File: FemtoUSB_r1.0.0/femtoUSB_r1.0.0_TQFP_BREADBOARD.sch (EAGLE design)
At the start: 26 parts, among them IC1 ATSAMD21E18A-AU

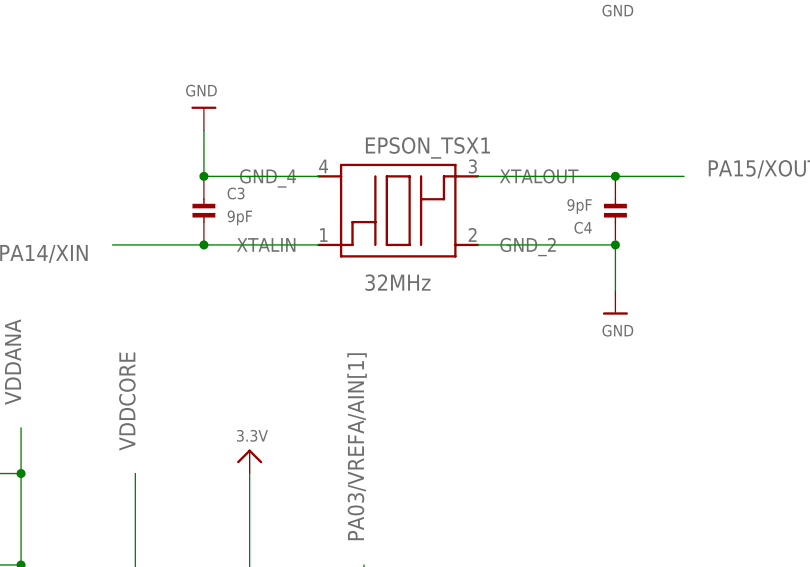
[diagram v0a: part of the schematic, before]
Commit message: Updating gerbers and BoM/Partslist of QFN version
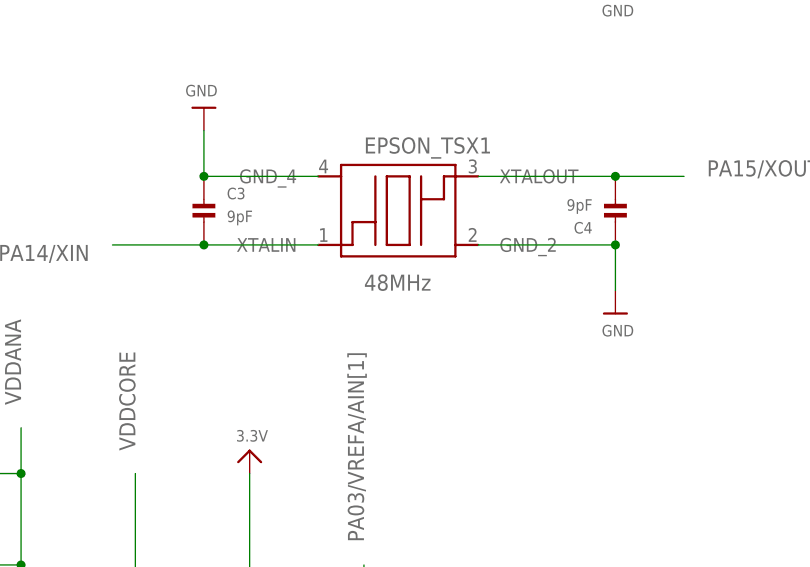
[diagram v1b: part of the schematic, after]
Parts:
- EPSON_TSX1: value 32MHz -> 48MHz
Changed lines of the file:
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@@
 <part name="U$24" library="microbuilder" deviceset="GND" device=""/>
 <part name="U$25" library="microbuilder" deviceset="GND" device=""/>
-<part name="EPSON_TSX1" library="crystals" deviceset="TSX-3225" device="" value="32MHz">
+<part name="EPSON_TSX1" library="crystals" deviceset="TSX-3225" device="" value="48MHz">
 <attribute name="DIGIKEY_PART" value="TSX-3225 32.0000MF15X-B-ND"/>
 </part>
